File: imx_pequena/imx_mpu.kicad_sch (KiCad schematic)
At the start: 0 parts

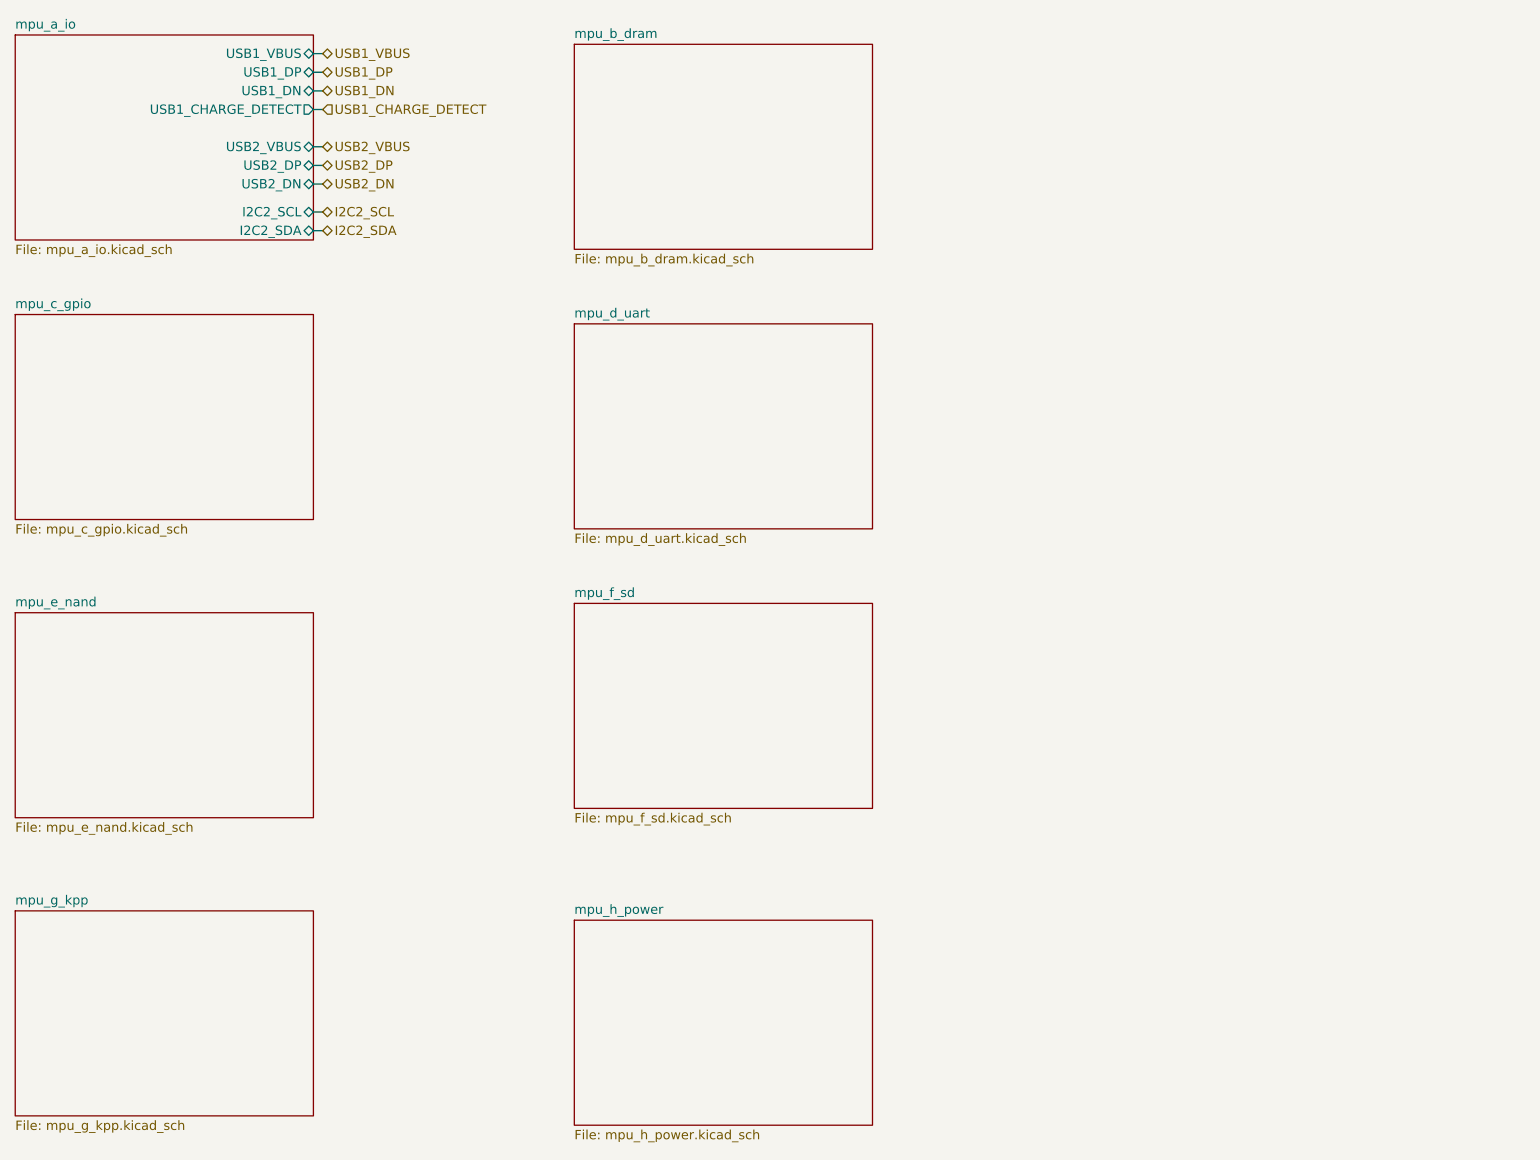
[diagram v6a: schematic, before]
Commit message: Updated pinouts
Added misc uart changes
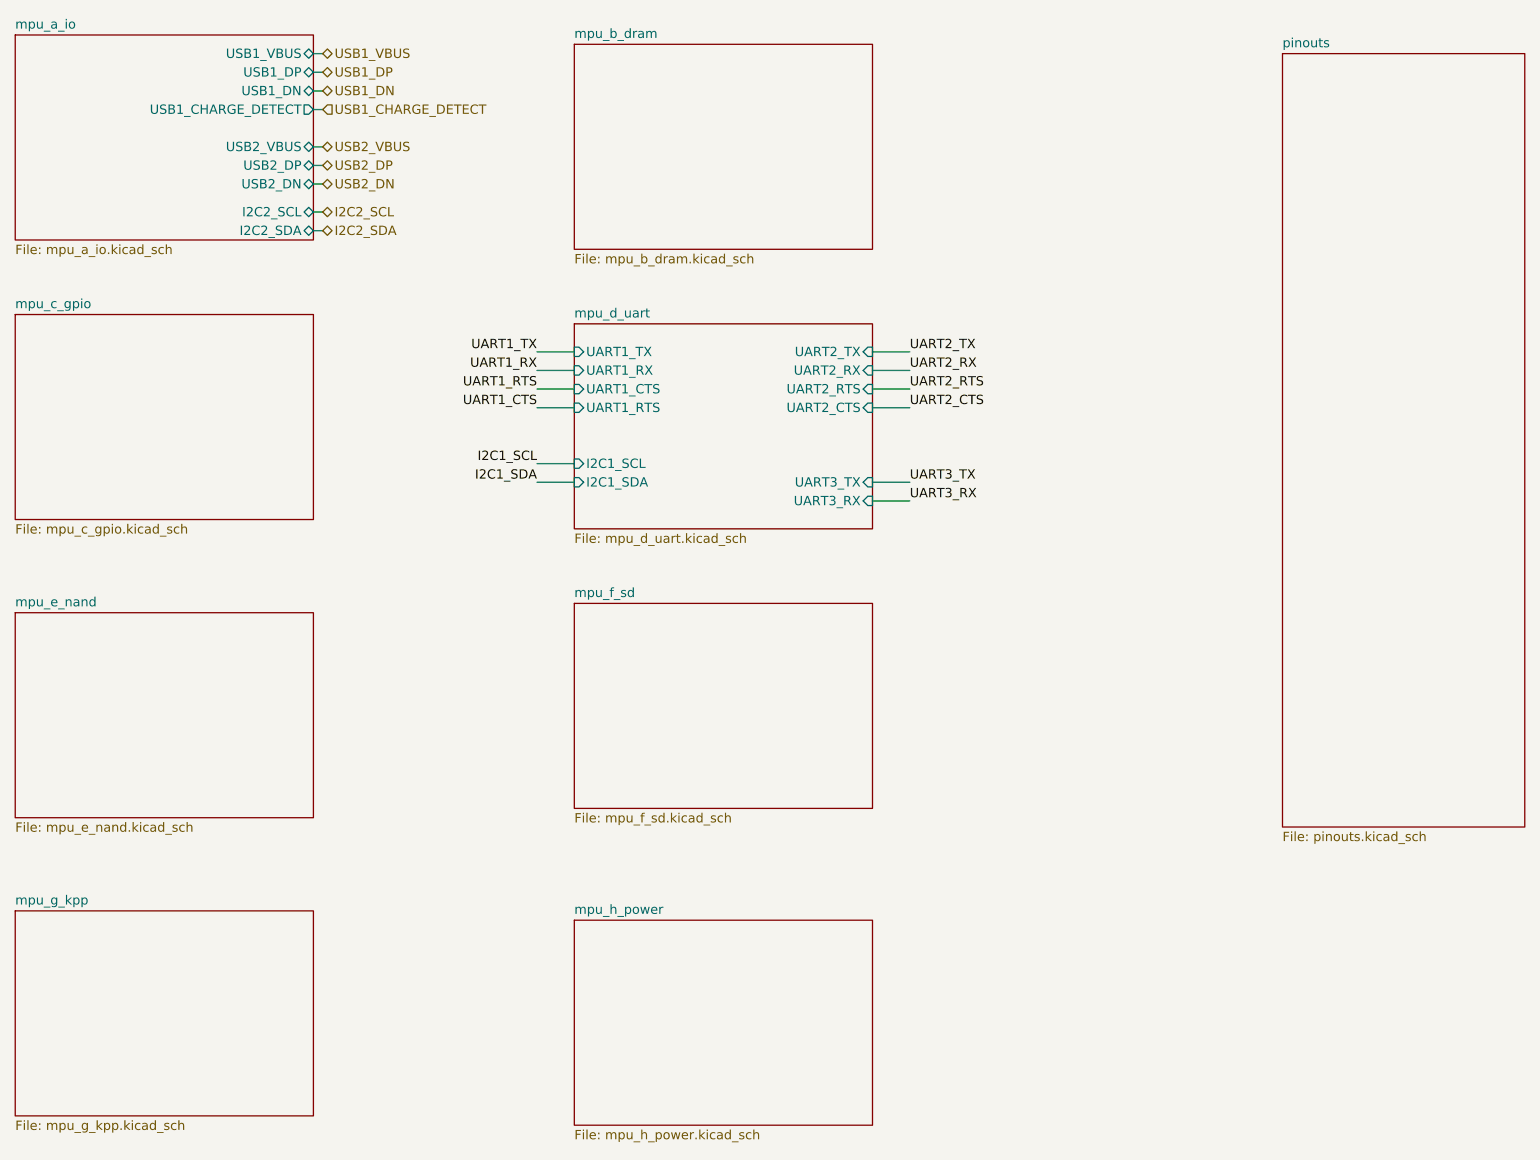
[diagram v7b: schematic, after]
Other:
- added sheet pinouts (pinouts.kicad_sch)
- sheet mpu_d_uart ports: added I2C1_SCL, I2C1_SDA, UART1_CTS, UART1_RTS, UART1_RX, UART1_TX, UART2_CTS, UART2_RTS, UART2_RX, UART2_TX, UART3_RX, UART3_TX; removed none
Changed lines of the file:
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@@
+    (stroke (width 0) (type default) (color 0 0 0 0))
+  )
+  (wire (pts (xy 147.32 93.98) (xy 152.4 93.98))
     (stroke (width 0) (type default) (color 0 0 0 0))
   )
@@
     (stroke (width 0) (type default) (color 0 0 0 0))
   )
+  (wire (pts (xy 147.32 73.66) (xy 152.4 73.66))
+    (stroke (width 0) (type default) (color 0 0 0 0))
+  )
+  (wire (pts (xy 147.32 78.74) (xy 152.4 78.74))
+    (stroke (width 0) (type default) (color 0 0 0 0))
+  )
+  (wire (pts (xy 147.32 91.44) (xy 152.4 91.44))
+    (stroke (width 0) (type default) (color 0 0 0 0))
+  )
   (wire (pts (xy 71.12 48.26) (xy 72.39 48.26))
     (stroke (width 0) (type default) (color 0 0 0 0))
@@
     (stroke (width 0) (type default) (color 0 0 0 0))
   )
+  (wire (pts (xy 101.6 76.2) (xy 106.68 76.2))
+    (stroke (width 0) (type default) (color 0 0 0 0))
+  )
+  (wire (pts (xy 101.6 81.28) (xy 106.68 81.28))
+    (stroke (width 0) (type default) (color 0 0 0 0))
+  )
+  (wire (pts (xy 101.6 91.44) (xy 106.68 91.44))
+    (stroke (width 0) (type default) (color 0 0 0 0))
+  )
+  (wire (pts (xy 147.32 81.28) (xy 152.4 81.28))
+    (stroke (width 0) (type default) (color 0 0 0 0))
+  )
   (wire (pts (xy 71.12 45.72) (xy 72.39 45.72))
     (stroke (width 0) (type default) (color 0 0 0 0))
@@
     (stroke (width 0) (type default) (color 0 0 0 0))
   )
+  (wire (pts (xy 101.6 73.66) (xy 106.68 73.66))
+    (stroke (width 0) (type default) (color 0 0 0 0))
+  )
   (wire (pts (xy 71.12 38.1) (xy 72.39 38.1))
     (stroke (width 0) (type default) (color 0 0 0 0))
   )
+  (wire (pts (xy 147.32 76.2) (xy 152.4 76.2))
+    (stroke (width 0) (type default) (color 0 0 0 0))
+  )
+  (wire (pts (xy 101.6 78.74) (xy 106.68 78.74))
+    (stroke (width 0) (type default) (color 0 0 0 0))
+  )
+  (wire (pts (xy 101.6 88.9) (xy 106.68 88.9))
+    (stroke (width 0) (type default) (color 0 0 0 0))
+  )
   (wire (pts (xy 71.12 50.8) (xy 72.39 50.8))
     (stroke (width 0) (type default) (color 0 0 0 0))
   )
+  (label "UART3_RX" (at 152.4 93.98 0)
+    (effects (font (size 1.27 1.27)) (justify left bottom))
+  )
+  (label "UART2_CTS" (at 152.4 81.28 0)
+    (effects (font (size 1.27 1.27)) (justify left bottom))
+  )
+  (label "UART1_RTS" (at 101.6 78.74 180)
+    (effects (font (size 1.27 1.27)) (justify right bottom))
+  )
+  (label "I2C1_SDA" (at 101.6 91.44 180)
+    (effects (font (size 1.27 1.27)) (justify right bottom))
+  )
+  (label "UART1_RX" (at 101.6 76.2 180)
+    (effects (font (size 1.27 1.27)) (justify right bottom))
+  )
+  (label "UART2_TX" (at 152.4 73.66 0)
+    (effects (font (size 1.27 1.27)) (justify left bottom))
+  )
+  (label "UART2_RTS" (at 152.4 78.74 0)
+    (effects (font (size 1.27 1.27)) (justify left bottom))
+  )
+  (label "I2C1_SCL" (at 101.6 88.9 180)
+    (effects (font (size 1.27 1.27)) (justify right bottom))
+  )
+  (label "UART3_TX" (at 152.4 91.44 0)
+    (effects (font (size 1.27 1.27)) (justify left bottom))
+  )
+  (label "UART1_CTS" (at 101.6 81.28 180)
+    (effects (font (size 1.27 1.27)) (justify right bottom))
+  )
+  (label "UART1_TX" (at 101.6 73.66 180)
+    (effects (font (size 1.27 1.27)) (justify right bottom))
+  )
+  (label "UART2_RX" (at 152.4 76.2 0)
+    (effects (font (size 1.27 1.27)) (justify left bottom))
+  )
   (hierarchical_label "USB1_DN" (shape bidirectional) (at 72.39 38.1 0)
     (effects (font (size 1.27 1.27)) (justify left))
@@
     )
   )
+  (sheet (at 203.2 33.02) (size 33.02 105.41) (fields_autoplaced)
+    (stroke (width 0.1524) (type solid) (color 0 0 0 0))
+    (fill (color 0 0 0 0.0000))
+    (property "Sheet name" "pinouts" (id 0) (at 203.2 32.3084 0)
+      (effects (font (size 1.27 1.27)) (justify left bottom))
+    )
+    (property "Sheet file" "pinouts.kicad_sch" (id 1) (at 203.2 139.0146 0)
+      (effects (font (size 1.27 1.27)) (justify left top))
+    )
+  )
   (sheet (at 30.48 68.58) (size 40.64 27.94) (fields_autoplaced)
     (stroke (width 0.1524) (type solid) (color 0 0 0 0))
@@
       (effects (font (size 1.27 1.27)) (justify left top))
     )
-  )
+    (pin "UART3_RX" input (at 147.32 93.98 0)
+      (effects (font (size 1.27 1.27)) (justify right))
+    )
+    (pin "UART3_TX" input (at 147.32 91.44 0)
+      (effects (font (size 1.27 1.27)) (justify right))
+    )
+    (pin "UART2_RX" input (at 147.32 76.2 0)
+      (effects (font (size 1.27 1.27)) (justify right))
+    )
+    (pin "UART2_TX" input (at 147.32 73.66 0)
+      (effects (font (size 1.27 1.27)) (justify right))
+    )
+    (pin "UART1_RX" input (at 106.68 76.2 180)
+      (effects (font (size 1.27 1.27)) (justify left))
+    )
+    (pin "UART1_TX" input (at 106.68 73.66 180)
+      (effects (font (size 1.27 1.27)) (justify left))
+    )
+    (pin "UART1_CTS" input (at 106.68 78.74 180)
+      (effects (font (size 1.27 1.27)) (justify left))
+    )
+    (pin "UART1_RTS" input (at 106.68 81.28 180)
+      (effects (font (size 1.27 1.27)) (justify left))
+    )
+    (pin "UART2_CTS" input (at 147.32 81.28 0)
+      (effects (font (size 1.27 1.27)) (justify right))
+    )
+    (pin "UART2_RTS" input (at 147.32 78.74 0)
+      (effects (font (size 1.27 1.27)) (justify right))
+    )
+    (pin "I2C1_SCL" input (at 106.68 88.9 180)
+      (effects (font (size 1.27 1.27)) (justify left))
+    )
+    (pin "I2C1_SDA" input (at 106.68 91.44 180)
+      (effects (font (size 1.27 1.27)) (justify left))
+    )
+  )

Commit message: Part Assignment
Assigned GPIOs and assigned footprints to most parts
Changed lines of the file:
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@@
 (kicad_sch (version 20211123) (generator eeschema)
   (paper "A4")
-  (wire (pts (xy 71.12 54.61) (xy 72.39 54.61))
+  (wire (pts (xy 71.12 57.15) (xy 76.2 57.15))
     (stroke (width 0) (type default) (color 0 0 0 0))
   )
   (wire (pts (xy 147.32 93.98) (xy 152.4 93.98))
-    (stroke (width 0) (type default) (color 0 0 0 0))
-  )
-  (wire (pts (xy 71.12 57.15) (xy 72.39 57.15))
     (stroke (width 0) (type default) (color 0 0 0 0))
   )
@@
   )
   (wire (pts (xy 147.32 81.28) (xy 152.4 81.28))
+    (stroke (width 0) (type default) (color 0 0 0 0))
+  )
+  (wire (pts (xy 71.12 54.61) (xy 76.2 54.61))
     (stroke (width 0) (type default) (color 0 0 0 0))
   )
@@
     (effects (font (size 1.27 1.27)) (justify left bottom))
   )
+  (label "I2C2_SDA" (at 76.2 57.15 0)
+    (effects (font (size 1.27 1.27)) (justify left bottom))
+  )
   (label "I2C1_SCL" (at 101.6 88.9 180)
     (effects (font (size 1.27 1.27)) (justify right bottom))
@@
     (effects (font (size 1.27 1.27)) (justify left bottom))
   )
+  (label "I2C2_SCL" (at 76.2 54.61 0)
+    (effects (font (size 1.27 1.27)) (justify left bottom))
+  )
   (hierarchical_label "USB1_DN" (shape bidirectional) (at 72.39 38.1 0)
-    (effects (font (size 1.27 1.27)) (justify left))
-  )
-  (hierarchical_label "I2C2_SCL" (shape bidirectional) (at 72.39 54.61 0)
     (effects (font (size 1.27 1.27)) (justify left))
   )
@@
     (effects (font (size 1.27 1.27)) (justify left))
   )
-  (hierarchical_label "I2C2_SDA" (shape bidirectional) (at 72.39 57.15 0)
-    (effects (font (size 1.27 1.27)) (justify left))
-  )
